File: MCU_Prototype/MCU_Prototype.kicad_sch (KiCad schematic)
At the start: 35 parts, among them J1 UART, J2 Battery, J3 SWD, J4 USB_A, J5 PIN1-PIN16, J6 PIN17-PIN32, J7 PIN33-PIN48, J8 PIN49-PIN64, SW1 SW_DPDT_x2, SW2 SW_Push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

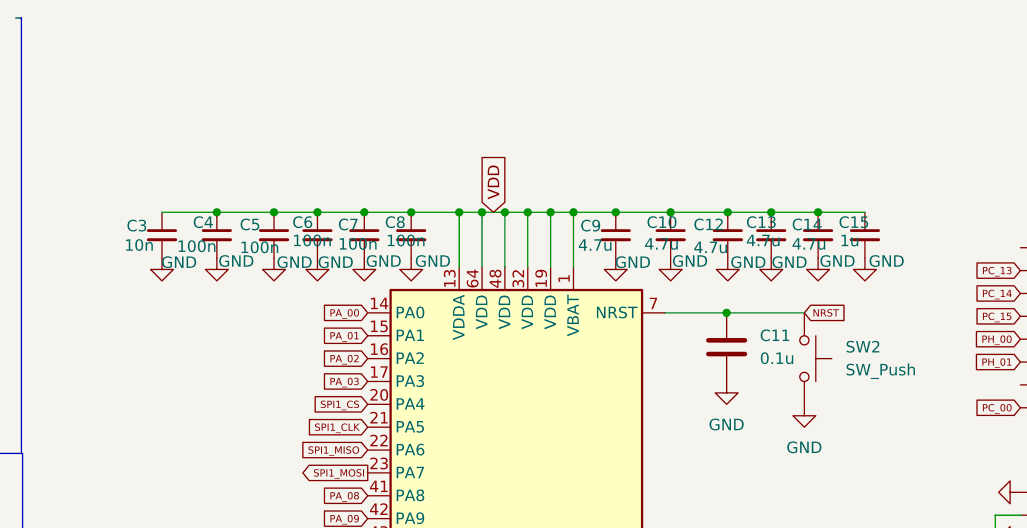
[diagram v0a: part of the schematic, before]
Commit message: Added silkscreen
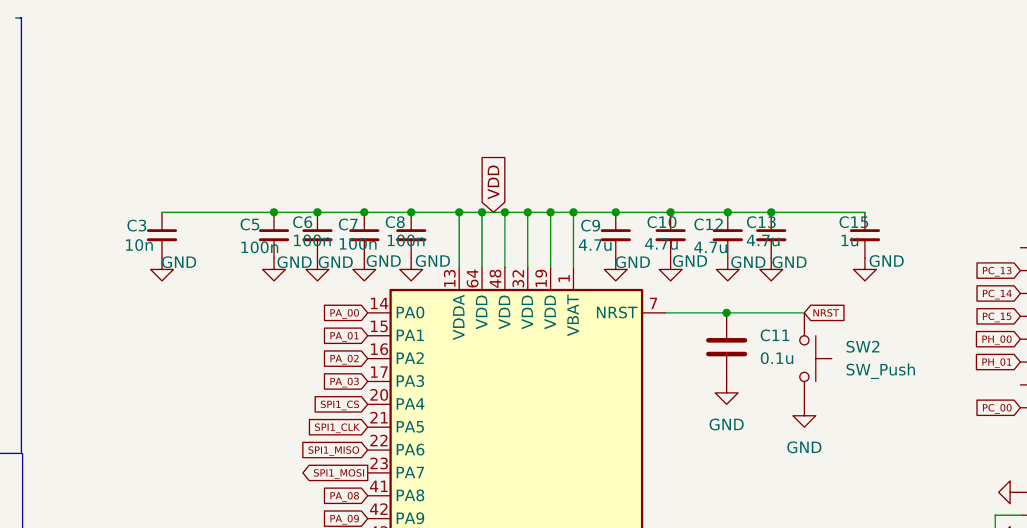
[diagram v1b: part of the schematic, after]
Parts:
- removed C14: 4.7u, Capacitor_THT:CP_Radial_D5.0mm_P2.00mm, symbol Device:C_Small
- removed C4: 100n, Capacitor_SMD:C_0805_2012Metric, symbol Device:C_Small
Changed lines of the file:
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@@
   (junction (at 30.226 162.56) (diameter 0) (color 0 0 0 0)
   )
-  (junction (at 109.855 33.274) (diameter 0) (color 0 0 0 0)
-  )
   (junction (at 149.479 33.274) (diameter 0) (color 0 0 0 0)
   )
@@
   (junction (at 144.399 136.398) (diameter 0) (color 0 0 0 0)
   )
-  (junction (at 176.657 33.274) (diameter 0) (color 0 0 0 0)
-  )
   (wire (pts (xy 159.639 44.45) (xy 166.497 44.45))
     (stroke (width 0) (type default) (color 0 0 0 0))
@@
     (stroke (width 0) (type default) (color 0 0 0 0))
   )
-  (wire (pts (xy 171.45 33.274) (xy 176.657 33.274))
+  (wire (pts (xy 171.45 33.274) (xy 181.864 33.274))
     (stroke (width 0) (type default) (color 0 0 0 0))
   )
@@
     (stroke (width 0) (type default) (color 0 0 0 0))
   )
-  (wire (pts (xy 176.657 33.274) (xy 181.864 33.274))
-    (stroke (width 0) (type default) (color 0 0 0 0))
-  )
   (polyline (pts (xy 88.265 60.071) (xy 88.265 91.059))
     (stroke (width 0) (type default) (color 0 0 0 0))
@@
     (stroke (width 0) (type default) (color 0 0 0 0))
   )
-  (wire (pts (xy 103.759 33.274) (xy 109.855 33.274))
+  (wire (pts (xy 103.759 33.274) (xy 116.205 33.274))
     (stroke (width 0) (type default) (color 0 0 0 0))
   )
@@
   )
   (wire (pts (xy 39.751 102.362) (xy 39.751 100.203))
-    (stroke (width 0) (type default) (color 0 0 0 0))
-  )
-  (wire (pts (xy 116.205 33.274) (xy 109.855 33.274))
     (stroke (width 0) (type default) (color 0 0 0 0))
   )
@@
     (pin "1")
   )
-  (symbol (lib_id "power:GND") (at 109.855 38.354 0) (unit 1)
-    (in_bom yes) (on_board yes)
-    (property "Reference" "#PWR0114" (id 0) (at 109.855 44.704 0)
-      (effects (font (size 1.27 1.27)) hide)
-    )
-    (property "Value" "GND" (id 1) (at 112.014 38.735 0))
-    (property "Footprint" "" (id 2) (at 109.855 38.354 0)
-      (effects (font (size 1.27 1.27)) hide)
-    )
-    (property "Datasheet" "" (id 3) (at 109.855 38.354 0)
-      (effects (font (size 1.27 1.27)) hide)
-    )
-    (pin "1")
-  )
   (symbol (lib_id "Device:Fuse") (at 81.661 148.463 0) (unit 1)
     (in_bom yes) (on_board yes) (fields_autoplaced)
@@
     )
     (property "Datasheet" "~" (id 3) (at 29.591 132.715 0)
-      (effects (font (size 1.27 1.27)) hide)
-    )
-    (pin "1")
-    (pin "2")
-  )
-  (symbol (lib_id "Device:C_Small") (at 176.657 35.814 0) (unit 1)
-    (in_bom yes) (on_board yes)
-    (property "Reference" "C14" (id 0) (at 173.736 34.671 0)
-      (effects (font (size 1.27 1.27)) (justify left))
-    )
-    (property "Value" "4.7u" (id 1) (at 173.736 36.83 0)
-      (effects (font (size 1.27 1.27)) (justify left))
-    )
-    (property "Footprint" "Capacitor_THT:CP_Radial_D5.0mm_P2.00mm" (id 2) (at 176.657 35.814 0)
-      (effects (font (size 1.27 1.27)) hide)
-    )
-    (property "Datasheet" "~" (id 3) (at 176.657 35.814 0)
       (effects (font (size 1.27 1.27)) hide)
     )
@@
     )
   )
-  (symbol (lib_id "Device:C_Small") (at 109.855 35.814 0) (unit 1)
-    (in_bom yes) (on_board yes)
-    (property "Reference" "C4" (id 0) (at 107.188 34.417 0)
-      (effects (font (size 1.27 1.27)) (justify left))
-    )
-    (property "Value" "100n" (id 1) (at 105.41 37.084 0)
-      (effects (font (size 1.27 1.27)) (justify left))
-    )
-    (property "Footprint" "Capacitor_SMD:C_0805_2012Metric" (id 2) (at 109.855 35.814 0)
-      (effects (font (size 1.27 1.27)) hide)
-    )
-    (property "Datasheet" "~" (id 3) (at 109.855 35.814 0)
-      (effects (font (size 1.27 1.27)) hide)
-    )
-    (pin "1")
-    (pin "2")
-  )
   (symbol (lib_id "Connector_Generic:Conn_02x08_Top_Bottom") (at 204.978 127.381 0) (unit 1)
     (in_bom yes) (on_board yes) (fields_autoplaced)
@@
     (pin "9")
   )
-  (symbol (lib_id "power:GND") (at 176.657 38.354 0) (unit 1)
-    (in_bom yes) (on_board yes)
-    (property "Reference" "#PWR0104" (id 0) (at 176.657 44.704 0)
-      (effects (font (size 1.27 1.27)) hide)
-    )
-    (property "Value" "GND" (id 1) (at 178.816 38.735 0))
-    (property "Footprint" "" (id 2) (at 176.657 38.354 0)
-      (effects (font (size 1.27 1.27)) hide)
-    )
-    (property "Datasheet" "" (id 3) (at 176.657 38.354 0)
-      (effects (font (size 1.27 1.27)) hide)
-    )
-    (pin "1")
-  )
   (sheet_instances
     (path "/" (page "1"))
@@
       (reference "#PWR0103") (unit 1) (value "GND") (footprint "")
     )
-    (path "/fe49d8c1-fc40-487c-9706-ced000b2d4ad"
-      (reference "#PWR0104") (unit 1) (value "GND") (footprint "")
-    )
     (path "/bb6ce214-b0c5-4b09-9d6e-e8bd21d997d1"
       (reference "#PWR0105") (unit 1) (value "GND") (footprint "")
@@
       (reference "#PWR0113") (unit 1) (value "GND") (footprint "")
     )
-    (path "/7a9637af-8cef-45a4-bc0c-4426fe151e68"
-      (reference "#PWR0114") (unit 1) (value "GND") (footprint "")
-    )
     (path "/71a3d07f-add3-41dd-a173-6fd47365365a"
       (reference "#PWR0115") (unit 1) (value "GND") (footprint "")
@@
       (reference "C3") (unit 1) (value "10n") (footprint "Capacitor_SMD:C_0805_2012Metric")
     )
-    (path "/f60bb931-00d1-4fce-a575-7cacf4fa738e"
-      (reference "C4") (unit 1) (value "100n") (footprint "Capacitor_SMD:C_0805_2012Metric")
-    )
     (path "/e9ec4e87-1d75-450d-9dc6-8995821fc267"
       (reference "C5") (unit 1) (value "100n") (footprint "Capacitor_SMD:C_0805_2012Metric")
@@
       (reference "C13") (unit 1) (value "4.7u") (footprint "Capacitor_THT:CP_Radial_D5.0mm_P2.00mm")
     )
-    (path "/ba0d5495-e1dd-4ae5-9f6a-826525866b5a"
-      (reference "C14") (unit 1) (value "4.7u") (footprint "Capacitor_THT:CP_Radial_D5.0mm_P2.00mm")
-    )
     (path "/0025cd73-2cc2-4a3e-ab89-42d4c7fdee89"
